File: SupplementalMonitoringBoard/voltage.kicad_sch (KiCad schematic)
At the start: 5 parts, among them U1 OPA842xDBV

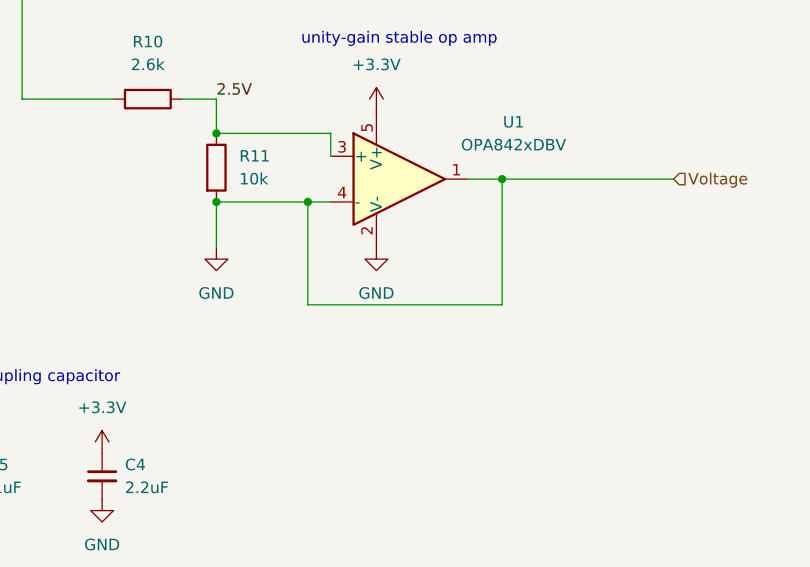
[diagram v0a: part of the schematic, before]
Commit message: Supplemental Monitoring Board Changes
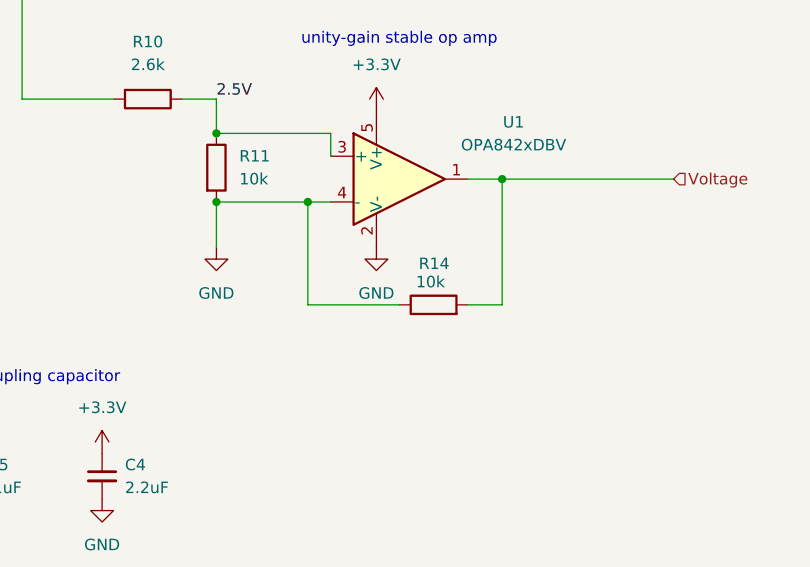
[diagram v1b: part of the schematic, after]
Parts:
- added R14: 10k, symbol Device:R
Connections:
- net GND: now also R14.1; no longer U1.1
- new net Voltage: R14.2, U1.1
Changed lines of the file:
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@@
+	(wire
+		(pts
+			(xy 129.54 118.11) (xy 139.7 118.11)
+		)
+		(stroke
+			(width 0)
+			(type default)
+		)
+	)
 	(wire
 		(pts
@@
 	(wire
 		(pts
-			(xy 129.54 118.11) (xy 151.13 118.11)
-		)
-		(stroke
-			(width 0)
-			(type default)
-		)
-	)
-	(wire
-		(pts
 			(xy 129.54 106.68) (xy 129.54 118.11)
 		)
@@
 		(pts
 			(xy 151.13 118.11) (xy 151.13 104.14)
+		)
+		(stroke
+			(width 0)
+			(type default)
+		)
+	)
+	(wire
+		(pts
+			(xy 147.32 118.11) (xy 151.13 118.11)
 		)
 		(stroke
@@
 					(unit 1)
 				)
+			)
+		)
+	)
+	(symbol
+		(lib_id "Device:R")
+		(at 143.51 118.11 90)
+		(unit 1)
+		(exclude_from_sim no)
+		(in_bom yes)
+		(on_board yes)
+		(dnp no)
+		(property "Reference" "R14"
+			(at 145.288 113.538 90)
+			(effects
+				(font
+					(size 1.27 1.27)
+				)
+				(justify left)
+			)
+		)
+		(property "Value" "10k"
+			(at 144.7799 115.57 90)
+			(effects
+				(font
+					(size 1.27 1.27)
+				)
+				(justify left)
+			)
+		)
+		(property "Footprint" ""
+			(at 143.51 119.888 90)
+			(effects
+				(font
+					(size 1.27 1.27)
+				)
+				(hide yes)
+			)
+		)
+		(property "Datasheet" "~"
+			(at 143.51 118.11 0)
+			(effects
+				(font
+					(size 1.27 1.27)
+				)
+				(hide yes)
+			)
+		)
+		(property "Description" "Resistor"
+			(at 143.51 118.11 0)
+			(effects
+				(font
+					(size 1.27 1.27)
+				)
+				(hide yes)
+			)
+		)
+		(pin "1"
+		)
+		(pin "2"
+		)
+		(instances
+			(project "SupplementalMonitoringBoard"
+				(path "/aa0415d0-3287-4bc4-9a8e-766ada9ace2f/c3517b11-42d4-41ac-8608-60dda8052ca3"
+					(reference "R14")
+					(unit 1)
+				)
